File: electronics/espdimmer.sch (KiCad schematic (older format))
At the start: 17 parts, among them J10 Screw_Terminal_01x02, J5 Conn_01x03, J6 Conn_01x02, J7 Screw_Terminal_01x02, J8 Screw_Terminal_01x02, J9 Screw_Terminal_01x02, Q1 IRLB3034, Q2 IRLB3034, SW1 SW_Push, SW2 SW_Push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

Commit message: PCB V1 (narrow)
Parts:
- removed C1: 100n, symbol Device:C_Small
- added C1: CP_Small, Capacitor_Tantalum_SMD:CP_EIA-3216-10_Kemet-I_Pad1.58x1.35mm_HandSolder, symbol Device:CP_Small
- J10: value Screw_Terminal_01x02 -> LED2; footprint (none) -> TerminalBlock:TerminalBlock_bornier-2_P5.08mm
- J5: value Conn_01x03 -> UART; footprint (none) -> Connector_PinHeader_2.54mm:PinHeader_1x03_P2.54mm_Vertical
- J6: value Conn_01x02 -> Motion; footprint (none) -> Connector_PinHeader_2.54mm:PinHeader_1x02_P2.54mm_Vertical
- J7: value Screw_Terminal_01x02 -> PWR1; footprint (none) -> TerminalBlock:TerminalBlock_bornier-2_P5.08mm
- J8: value Screw_Terminal_01x02 -> PWR2; footprint (none) -> TerminalBlock:TerminalBlock_bornier-2_P5.08mm
- J9: value Screw_Terminal_01x02 -> LED1; footprint (none) -> TerminalBlock:TerminalBlock_bornier-2_P5.08mm
- PS1: footprint (none) -> ESPDimmer:XM1584_buck_module
- Q1, Q2: footprint (none) -> Package_TO_SOT_THT:TO-220-3_Vertical
- R1, R2, R3, R4: footprint (none) -> Resistor_SMD:R_0805_2012Metric_Pad1.15x1.40mm_HandSolder
- SW1: value SW_Push -> Reset; footprint (none) -> Button_Switch_THT:SW_PUSH_6mm
- SW2: value SW_Push -> Flash; footprint (none) -> Button_Switch_THT:SW_PUSH_6mm
- U1: footprint (none) -> ESP8266:ESP-01
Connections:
- net labels added: GNDD
- wire segments 64 -> 66
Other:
- moved on the sheet: J10
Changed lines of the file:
@@
 F 0 "U1" H 5600 3850 50  0000 C CNN
 F 1 "ESP-01v090" H 5600 3650 50  0000 C CNN
-F 2 "" H 5600 3700 50  0001 C CNN
+F 2 "ESP8266:ESP-01" H 5600 3700 50  0001 C CNN
 F 3 "http://l0l.org.uk/2014/12/esp8266-modules-hardware-guide-gotta-catch-em-all/" H 5600 3700 50  0001 C CNN
 	1    5600 3700
@@
 F 0 "Q1" H 7504 4096 50  0000 L CNN
 F 1 "IRLB3034" H 7000 4250 50  0000 L CNN
-F 2 "" H 7500 4150 50  0001 C CNN
+F 2 "Package_TO_SOT_THT:TO-220-3_Vertical" H 7500 4150 50  0001 C CNN
 F 3 "~" H 7300 4050 50  0001 C CNN
 	1    7300 4050
@@
 F 0 "Q2" H 7750 3900 50  0000 L CNN
 F 1 "IRLB3034" H 7800 4300 50  0000 L CNN
-F 2 "" H 8100 4150 50  0001 C CNN
+F 2 "Package_TO_SOT_THT:TO-220-3_Vertical" H 8100 4150 50  0001 C CNN
 F 3 "~" H 7900 4050 50  0001 C CNN
 	1    7900 4050
@@
 F 0 "R3" H 7009 3296 50  0000 L CNN
 F 1 "10k" H 7009 3205 50  0000 L CNN
-F 2 "" H 6950 3250 50  0001 C CNN
+F 2 "Resistor_SMD:R_0805_2012Metric_Pad1.15x1.40mm_HandSolder" H 6950 3250 50  0001 C CNN
 F 3 "~" H 6950 3250 50  0001 C CNN
 	1    6950 3250
@@
 F 0 "R4" H 7709 3296 50  0000 L CNN
 F 1 "10k" H 7709 3205 50  0000 L CNN
-F 2 "" H 7650 3250 50  0001 C CNN
+F 2 "Resistor_SMD:R_0805_2012Metric_Pad1.15x1.40mm_HandSolder" H 7650 3250 50  0001 C CNN
 F 3 "~" H 7650 3250 50  0001 C CNN
 	1    7650 3250
@@
 Wire Wire Line
 	6950 2950 6950 3150
-$Comp
-L power:GND #PWR012
-U 1 1 5FDF4073
-P 7400 4550
-F 0 "#PWR012" H 7400 4300 50  0001 C CNN
-F 1 "GND" H 7405 4377 50  0000 C CNN
-F 2 "" H 7400 4550 50  0001 C CNN
-F 3 "" H 7400 4550 50  0001 C CNN
-	1    7400 4550
-	1    0    0    -1
-$EndComp
-$Comp
-L power:GND #PWR014
-U 1 1 5FDF454A
-P 8000 4550
-F 0 "#PWR014" H 8000 4300 50  0001 C CNN
-F 1 "GND" H 8005 4377 50  0000 C CNN
-F 2 "" H 8000 4550 50  0001 C CNN
-F 3 "" H 8000 4550 50  0001 C CNN
-	1    8000 4550
-	1    0    0    -1
-$EndComp
-Wire Wire Line
-	7400 4250 7400 4550
-$Comp
-L power:GND #PWR03
-U 1 1 5FE22A75
-P 3550 4550
-F 0 "#PWR03" H 3550 4300 50  0001 C CNN
-F 1 "GND" H 3555 4377 50  0000 C CNN
-F 2 "" H 3550 4550 50  0001 C CNN
-F 3 "" H 3550 4550 50  0001 C CNN
-	1    3550 4550
-	1    0    0    -1
-$EndComp
+Wire Wire Line
+	7400 4250 7400 4400
 $Comp
 L power:GND #PWR02
 U 1 1 5FE2314A
-P 2650 4550
-F 0 "#PWR02" H 2650 4300 50  0001 C CNN
-F 1 "GND" H 2655 4377 50  0000 C CNN
-F 2 "" H 2650 4550 50  0001 C CNN
-F 3 "" H 2650 4550 50  0001 C CNN
-	1    2650 4550
-	1    0    0    -1
-$EndComp
-Wire Wire Line
-	2650 3850 2650 4550
-Wire Wire Line
-	3550 3850 3550 4550
-$Comp
-L Connector:Screw_Terminal_01x02 J8
-U 1 1 5FE24A4C
-P 8700 3050
-F 0 "J8" H 8850 3000 50  0000 C CNN
-F 1 "Screw_Terminal_01x02" H 8618 3176 50  0001 C CNN
-F 2 "" H 8700 3050 50  0001 C CNN
-F 3 "~" H 8700 3050 50  0001 C CNN
-	1    8700 3050
-	1    0    0    -1
-$EndComp
-$Comp
-L power:GND #PWR015
-U 1 1 5FE25B65
-P 8450 4550
-F 0 "#PWR015" H 8450 4300 50  0001 C CNN
-F 1 "GND" H 8455 4377 50  0000 C CNN
-F 2 "" H 8450 4550 50  0001 C CNN
-F 3 "" H 8450 4550 50  0001 C CNN
-	1    8450 4550
-	1    0    0    -1
-$EndComp
-$Comp
-L Device:C_Small C1
-U 1 1 5FE1F45B
-P 3750 4150
-F 0 "C1" H 3900 4100 50  0000 R CNN
-F 1 "100n" H 3950 4250 50  0000 R CNN
-F 2 "" H 3750 4150 50  0001 C CNN
-F 3 "~" H 3750 4150 50  0001 C CNN
-	1    3750 4150
-	1    0    0    1
-$EndComp
+P 3150 4550
+F 0 "#PWR02" H 3150 4300 50  0001 C CNN
+F 1 "GND" H 3155 4377 50  0000 C CNN
+F 2 "" H 3150 4550 50  0001 C CNN
+F 3 "" H 3150 4550 50  0001 C CNN
+	1    3150 4550
+	1    0    0    -1
+$EndComp
+Wire Wire Line
+	3150 4050 3150 4550
 $Comp
 L power:GND #PWR05
@@
 F 0 "R1" H 4059 3696 50  0000 L CNN
 F 1 "10k" H 4059 3605 50  0000 L CNN
-F 2 "" H 4000 3650 50  0001 C CNN
+F 2 "Resistor_SMD:R_0805_2012Metric_Pad1.15x1.40mm_HandSolder" H 4000 3650 50  0001 C CNN
 F 3 "~" H 4000 3650 50  0001 C CNN
 	1    4000 3650
@@
 F 0 "R2" H 4500 3800 50  0000 L CNN
 F 1 "10k" H 4500 3700 50  0000 L CNN
-F 2 "" H 4350 3750 50  0001 C CNN
+F 2 "Resistor_SMD:R_0805_2012Metric_Pad1.15x1.40mm_HandSolder" H 4350 3750 50  0001 C CNN
 F 3 "~" H 4350 3750 50  0001 C CNN
 	1    4350 3750
@@
 P 4550 4300
 F 0 "SW1" V 4504 4252 50  0000 R CNN
-F 1 "SW_Push" V 4595 4252 50  0001 R CNN
-F 2 "" H 4550 4500 50  0001 C CNN
+F 1 "Reset" V 4595 4252 50  0000 R CNN
+F 2 "Button_Switch_THT:SW_PUSH_6mm" H 4550 4500 50  0001 C CNN
 F 3 "~" H 4550 4500 50  0001 C CNN
 	1    4550 4300
@@
 L Connector:Screw_Terminal_01x02 J9
 U 1 1 5FE61684
-P 8700 3350
-F 0 "J9" H 8850 3300 50  0000 C CNN
-F 1 "Screw_Terminal_01x02" H 8618 3476 50  0001 C CNN
-F 2 "" H 8700 3350 50  0001 C CNN
-F 3 "~" H 8700 3350 50  0001 C CNN
-	1    8700 3350
-	1    0    0    -1
+P 8700 3450
+F 0 "J9" H 8850 3350 50  0000 C CNN
+F 1 "LED1" H 8900 3450 50  0000 C CNN
+F 2 "TerminalBlock:TerminalBlock_bornier-2_P5.08mm" H 8700 3450 50  0001 C CNN
+F 3 "~" H 8700 3450 50  0001 C CNN
+	1    8700 3450
+	1    0    0    1
 $EndComp
 $Comp
@@
 U 1 1 5FE62049
 P 8700 3750
-F 0 "J10" H 8850 3700 50  0000 C CNN
-F 1 "Screw_Terminal_01x02" H 8618 3876 50  0001 C CNN
-F 2 "" H 8700 3750 50  0001 C CNN
+F 0 "J10" H 8900 3650 50  0000 C CNN
+F 1 "LED2" H 8900 3750 50  0000 C CNN
+F 2 "TerminalBlock:TerminalBlock_bornier-2_P5.08mm" H 8700 3750 50  0001 C CNN
 F 3 "~" H 8700 3750 50  0001 C CNN
 	1    8700 3750
-	1    0    0    -1
+	1    0    0    1
 $EndComp
 $Comp
@@
 P 6950 4300
 F 0 "SW2" V 6904 4252 50  0000 R CNN
-F 1 "SW_Push" V 6995 4252 50  0001 R CNN
-F 2 "" H 6950 4500 50  0001 C CNN
+F 1 "Flash" V 6995 4252 50  0000 R CNN
+F 2 "Button_Switch_THT:SW_PUSH_6mm" H 6950 4500 50  0001 C CNN
 F 3 "~" H 6950 4500 50  0001 C CNN
 	1    6950 4300
@@
 	6950 4100 6950 4050
 Connection ~ 6950 4050
-Wire Wire Line
-	8500 3850 8000 3850
 Wire Wire Line
 	8500 3450 7400 3450
@@
 P 6150 2700
 F 0 "J6" V 6250 2650 50  0000 C CNN
-F 1 "Conn_01x02" H 6300 2850 50  0001 C CNN
-F 2 "" H 6150 2700 50  0001 C CNN
+F 1 "Motion" V 6150 2900 50  0000 C CNN
+F 2 "Connector_PinHeader_2.54mm:PinHeader_1x02_P2.54mm_Vertical" H 6150 2700 50  0001 C CNN
 F 3 "~" H 6150 2700 50  0001 C CNN
 	1    6150 2700
@@
 Connection ~ 8450 3150
 Wire Wire Line
-	8500 3750 8350 3750
-Wire Wire Line
-	8350 3750 8350 3050
+	8500 3650 8350 3650
+Wire Wire Line
+	8350 3650 8350 3050
 Wire Wire Line
 	8350 3050 8500 3050
@@
 P 5650 2700
 F 0 "J5" V 5750 2750 50  0000 R CNN
-F 1 "Conn_01x03" V 5523 2512 50  0001 R CNN
-F 2 "" H 5650 2700 50  0001 C CNN
+F 1 "UART" V 5650 3100 50  0000 R CNN
+F 2 "Connector_PinHeader_2.54mm:PinHeader_1x03_P2.54mm_Vertical" H 5650 2700 50  0001 C CNN
 F 3 "~" H 5650 2700 50  0001 C CNN
 	1    5650 2700
@@
 L Connector:Screw_Terminal_01x02 J7
 U 1 1 5FF5CAAF
-P 8700 2750
-F 0 "J7" H 8850 2700 50  0000 C CNN
-F 1 "Screw_Terminal_01x02" H 8618 2876 50  0001 C CNN
-F 2 "" H 8700 2750 50  0001 C CNN
-F 3 "~" H 8700 2750 50  0001 C CNN
-	1    8700 2750
-	1    0    0    -1
+P 8700 2850
+F 0 "J7" H 8850 2750 50  0000 C CNN
+F 1 "PWR1" H 8900 2850 50  0000 C CNN
+F 2 "TerminalBlock:TerminalBlock_bornier-2_P5.08mm" H 8700 2850 50  0001 C CNN
+F 3 "~" H 8700 2850 50  0001 C CNN
+	1    8700 2850
+	1    0    0    1
 $EndComp
 Wire Wire Line
@@
 F 0 "PS1" H 3150 4117 50  0000 C CNN
 F 1 "BUCK" H 3150 4026 50  0000 C CNN
-F 2 "" H 2100 3500 50  0001 L CNN
+F 2 "ESPDimmer:XM1584_buck_module" H 2100 3500 50  0001 L CNN
 F 3 "" H 4200 3450 50  0001 L CNN
 	1    3150 3750
@@
 $EndComp
 Wire Wire Line
-	2650 3850 2750 3850
-Wire Wire Line
 	2650 3050 8250 3050
 Wire Wire Line
@@
 Wire Wire Line
 	8250 3050 8250 2750
+$Comp
+L Device:CP_Small C1
+U 1 1 5FFA4758
+P 3750 4150
+F 0 "C1" H 3838 4196 50  0000 L CNN
+F 1 "CP_Small" H 3838 4105 50  0000 L CNN
+F 2 "Capacitor_Tantalum_SMD:CP_EIA-3216-10_Kemet-I_Pad1.58x1.35mm_HandSolder" H 3750 4150 50  0001 C CNN
+F 3 "~" H 3750 4150 50  0001 C CNN
+	1    3750 4150
+	1    0    0    -1
+$EndComp
+Wire Wire Line
+	8500 3750 8000 3750
+Wire Wire Line
+	8000 3750 8000 3850
+$Comp
+L Connector:Screw_Terminal_01x02 J8
+U 1 1 5FE24A4C
+P 8700 3150
+F 0 "J8" H 8850 3050 50  0000 C CNN
+F 1 "PWR2" H 8900 3150 50  0000 C CNN
+F 2 "TerminalBlock:TerminalBlock_bornier-2_P5.08mm" H 8700 3150 50  0001 C CNN
+F 3 "~" H 8700 3150 50  0001 C CNN
+	1    8700 3150
+	1    0    0    1
+$EndComp
+$Comp
+L power:GNDD #PWR0101
+U 1 1 5FFD72B4
+P 7400 4550
+F 0 "#PWR0101" H 7400 4300 50  0001 C CNN
+F 1 "GNDD" H 7404 4395 50  0000 C CNN
+F 2 "" H 7400 4550 50  0001 C CNN
+F 3 "" H 7400 4550 50  0001 C CNN
+	1    7400 4550
+	1    0    0    -1
+$EndComp
+$Comp
+L power:GNDD #PWR0102
+U 1 1 5FFD779F
+P 8000 4550
+F 0 "#PWR0102" H 8000 4300 50  0001 C CNN
+F 1 "GNDD" H 8004 4395 50  0000 C CNN
+F 2 "" H 8000 4550 50  0001 C CNN
+F 3 "" H 8000 4550 50  0001 C CNN
+	1    8000 4550
+	1    0    0    -1
+$EndComp
+$Comp
+L power:GNDD #PWR0103
+U 1 1 5FFD7CBE
+P 8450 4550
+F 0 "#PWR0103" H 8450 4300 50  0001 C CNN
+F 1 "GNDD" H 8454 4395 50  0000 C CNN
+F 2 "" H 8450 4550 50  0001 C CNN
+F 3 "" H 8450 4550 50  0001 C CNN
+	1    8450 4550
+	1    0    0    -1
+$EndComp
+$Comp
+L power:GND #PWR0104
+U 1 1 5FFD8056
+P 7200 4550
+F 0 "#PWR0104" H 7200 4300 50  0001 C CNN
+F 1 "GND" H 7205 4377 50  0000 C CNN
+F 2 "" H 7200 4550 50  0001 C CNN
+F 3 "" H 7200 4550 50  0001 C CNN
+	1    7200 4550
+	1    0    0    -1
+$EndComp
+Wire Wire Line
+	7200 4550 7200 4400
+Wire Wire Line
+	7200 4400 7400 4400
+Connection ~ 7400 4400
+Wire Wire Line
+	7400 4400 7400 4550
 $EndSCHEMATC

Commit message: Schematics and PCB design updated
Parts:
- removed PS1: BUCK, ESPDimmer:XM1584_buck_module, symbol buck:BUCK
- added PS1: BUCK_4P, Buck:XM1584_buck_mod_4p, symbol Buck:BUCK_4P
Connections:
- net labels added: PWR1, PWR2
- wire segments 66 -> 64
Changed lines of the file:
@@
 Wire Wire Line
 	6950 2950 6950 3150
-Wire Wire Line
-	7400 4250 7400 4400
 $Comp
 L power:GND #PWR02
 U 1 1 5FE2314A
-P 3150 4550
-F 0 "#PWR02" H 3150 4300 50  0001 C CNN
-F 1 "GND" H 3155 4377 50  0000 C CNN
-F 2 "" H 3150 4550 50  0001 C CNN
-F 3 "" H 3150 4550 50  0001 C CNN
-	1    3150 4550
-	1    0    0    -1
-$EndComp
-Wire Wire Line
-	3150 4050 3150 4550
+P 3550 4550
+F 0 "#PWR02" H 3550 4300 50  0001 C CNN
+F 1 "GND" H 3555 4377 50  0000 C CNN
+F 2 "" H 3550 4550 50  0001 C CNN
+F 3 "" H 3550 4550 50  0001 C CNN
+	1    3550 4550
+	1    0    0    -1
+$EndComp
+Wire Wire Line
+	3550 3850 3550 4550
 $Comp
 L power:GND #PWR05
@@
 Wire Wire Line
 	2650 3050 2650 3650
-$Comp
-L buck:BUCK PS1
-U 1 1 5FF86192
-P 3150 3750
-F 0 "PS1" H 3150 4117 50  0000 C CNN
-F 1 "BUCK" H 3150 4026 50  0000 C CNN
-F 2 "ESPDimmer:XM1584_buck_module" H 2100 3500 50  0001 L CNN
-F 3 "" H 4200 3450 50  0001 L CNN
-	1    3150 3750
-	1    0    0    -1
-$EndComp
 Wire Wire Line
 	2650 3050 8250 3050
@@
 $EndComp
 $Comp
-L power:GND #PWR0104
-U 1 1 5FFD8056
-P 7200 4550
-F 0 "#PWR0104" H 7200 4300 50  0001 C CNN
-F 1 "GND" H 7205 4377 50  0000 C CNN
-F 2 "" H 7200 4550 50  0001 C CNN
-F 3 "" H 7200 4550 50  0001 C CNN
-	1    7200 4550
-	1    0    0    -1
-$EndComp
-Wire Wire Line
-	7200 4550 7200 4400
-Wire Wire Line
-	7200 4400 7400 4400
-Connection ~ 7400 4400
-Wire Wire Line
-	7400 4400 7400 4550
+L Buck:BUCK_4P PS1
+U 1 1 6006370D
+P 3150 3750
+F 0 "PS1" H 3150 4117 50  0000 C CNN
+F 1 "BUCK_4P" H 3150 4026 50  0000 C CNN
+F 2 "Buck:XM1584_buck_mod_4p" H 2100 3500 50  0001 L CNN
+F 3 "" H 4200 3450 50  0001 L CNN
+	1    3150 3750
+	1    0    0    -1
+$EndComp
+$Comp
+L power:GNDD #PWR0105
+U 1 1 60068775
+P 2750 4550
+F 0 "#PWR0105" H 2750 4300 50  0001 C CNN
+F 1 "GNDD" H 2754 4395 50  0000 C CNN
+F 2 "" H 2750 4550 50  0001 C CNN
+F 3 "" H 2750 4550 50  0001 C CNN
+	1    2750 4550
+	1    0    0    -1
+$EndComp
+Wire Wire Line
+	2750 3850 2750 4550
+Wire Wire Line
+	7400 4250 7400 4550
+Text Label 8250 2750 0    50   ~ 0
+PWR1
+Text Label 8350 3050 3    50   ~ 0
+PWR2
 $EndSCHEMATC

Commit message: Schematics/PCB updated
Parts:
- added R5: 4.7k, Resistor_SMD:R_0805_2012Metric_Pad1.15x1.40mm_HandSolder, symbol Device:R_Small
- R3, R4: value 10k -> 4.7k
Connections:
- wire segments 64 -> 66
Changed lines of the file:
@@
 P 6950 3250
 F 0 "R3" H 7009 3296 50  0000 L CNN
-F 1 "10k" H 7009 3205 50  0000 L CNN
+F 1 "4.7k" H 7009 3205 50  0000 L CNN
 F 2 "Resistor_SMD:R_0805_2012Metric_Pad1.15x1.40mm_HandSolder" H 6950 3250 50  0001 C CNN
 F 3 "~" H 6950 3250 50  0001 C CNN
@@
 P 7650 3250
 F 0 "R4" H 7709 3296 50  0000 L CNN
-F 1 "10k" H 7709 3205 50  0000 L CNN
+F 1 "4.7k" H 7709 3205 50  0000 L CNN
 F 2 "Resistor_SMD:R_0805_2012Metric_Pad1.15x1.40mm_HandSolder" H 7650 3250 50  0001 C CNN
 F 3 "~" H 7650 3250 50  0001 C CNN
@@
 Text Label 8350 3050 3    50   ~ 0
 PWR2
+$Comp
+L Device:R_Small R5
+U 1 1 600883F6
+P 6800 2950
+F 0 "R5" H 6859 2996 50  0000 L CNN
+F 1 "4.7k" H 6859 2905 50  0000 L CNN
+F 2 "Resistor_SMD:R_0805_2012Metric_Pad1.15x1.40mm_HandSolder" H 6800 2950 50  0001 C CNN
+F 3 "~" H 6800 2950 50  0001 C CNN
+	1    6800 2950
+	0    1    -1   0
+$EndComp
+Wire Wire Line
+	6650 2950 6700 2950
+Connection ~ 6650 2950
+Wire Wire Line
+	6900 2950 6950 2950
 $EndSCHEMATC

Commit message: esphome config added
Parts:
- added C2: 100nF 50V, Capacitor_SMD:C_0805_2012Metric_Pad1.15x1.40mm_HandSolder, symbol Device:C_Small
- added D1: SS14, Diode_SMD:D_SMA_Handsoldering, symbol Device:D_Small
- C1: value CP_Small -> 10uF 10V
- U1: symbol ESP-8266:ESP-01v090 -> espdimmer-rescue:ESP-01v090-ESP-8266
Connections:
- net labels removed: GNDD
- wire segments 66 -> 69
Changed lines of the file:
@@
 $EndDescr
 $Comp
-L ESP-8266:ESP-01v090 U1
+L espdimmer-rescue:ESP-01v090-ESP-8266 U1
 U 1 1 5FDE3173
 P 5600 3700
@@
 	1    0    0    -1
 $EndComp
-Wire Wire Line
-	3550 3850 3550 4550
 $Comp
 L power:GND #PWR05
@@
 	4100 3650 4650 3650
 Wire Wire Line
-	2650 3650 2750 3650
+	2500 3650 2750 3650
 Wire Wire Line
 	6950 3750 6950 4050
@@
 $EndComp
 Wire Wire Line
-	2650 3050 2650 3650
-Wire Wire Line
-	2650 3050 8250 3050
+	2500 3050 2500 3650
+Wire Wire Line
+	2500 3050 7900 3050
 Wire Wire Line
 	8250 3350 8250 3050
@@
 P 3750 4150
 F 0 "C1" H 3838 4196 50  0000 L CNN
-F 1 "CP_Small" H 3838 4105 50  0000 L CNN
+F 1 "10uF 10V" H 3838 4105 50  0000 L CNN
 F 2 "Capacitor_Tantalum_SMD:CP_EIA-3216-10_Kemet-I_Pad1.58x1.35mm_HandSolder" H 3750 4150 50  0001 C CNN
 F 3 "~" H 3750 4150 50  0001 C CNN
@@
 $EndComp
 $Comp
-L power:GNDD #PWR0101
-U 1 1 5FFD72B4
-P 7400 4550
-F 0 "#PWR0101" H 7400 4300 50  0001 C CNN
-F 1 "GNDD" H 7404 4395 50  0000 C CNN
-F 2 "" H 7400 4550 50  0001 C CNN
-F 3 "" H 7400 4550 50  0001 C CNN
-	1    7400 4550
-	1    0    0    -1
-$EndComp
-$Comp
-L power:GNDD #PWR0102
-U 1 1 5FFD779F
-P 8000 4550
-F 0 "#PWR0102" H 8000 4300 50  0001 C CNN
-F 1 "GNDD" H 8004 4395 50  0000 C CNN
-F 2 "" H 8000 4550 50  0001 C CNN
-F 3 "" H 8000 4550 50  0001 C CNN
-	1    8000 4550
-	1    0    0    -1
-$EndComp
-$Comp
-L power:GNDD #PWR0103
-U 1 1 5FFD7CBE
-P 8450 4550
-F 0 "#PWR0103" H 8450 4300 50  0001 C CNN
-F 1 "GNDD" H 8454 4395 50  0000 C CNN
-F 2 "" H 8450 4550 50  0001 C CNN
-F 3 "" H 8450 4550 50  0001 C CNN
-	1    8450 4550
-	1    0    0    -1
-$EndComp
-$Comp
 L Buck:BUCK_4P PS1
 U 1 1 6006370D
@@
 	1    0    0    -1
 $EndComp
-$Comp
-L power:GNDD #PWR0105
-U 1 1 60068775
-P 2750 4550
-F 0 "#PWR0105" H 2750 4300 50  0001 C CNN
-F 1 "GNDD" H 2754 4395 50  0000 C CNN
-F 2 "" H 2750 4550 50  0001 C CNN
-F 3 "" H 2750 4550 50  0001 C CNN
-	1    2750 4550
-	1    0    0    -1
-$EndComp
-Wire Wire Line
-	2750 3850 2750 4550
 Wire Wire Line
 	7400 4250 7400 4550
@@
 Wire Wire Line
 	6900 2950 6950 2950
+$Comp
+L Device:D_Small D1
+U 1 1 600C3ECC
+P 8000 3050
+F 0 "D1" H 8000 3255 50  0000 C CNN
+F 1 "SS14" H 8000 3164 50  0000 C CNN
+F 2 "Diode_SMD:D_SMA_Handsoldering" V 8000 3050 50  0001 C CNN
+F 3 "~" V 8000 3050 50  0001 C CNN
+	1    8000 3050
+	1    0    0    -1
+$EndComp
+Wire Wire Line
+	8100 3050 8250 3050
+Wire Wire Line
+	2500 4050 2500 3650
+Connection ~ 2500 3650
+Wire Wire Line
+	2500 4550 2500 4250
+$Comp
+L Device:C_Small C2
+U 1 1 600E829E
+P 2500 4150
+F 0 "C2" H 2592 4196 50  0000 L CNN
+F 1 "100nF 50V" H 2250 4050 50  0000 L CNN
+F 2 "Capacitor_SMD:C_0805_2012Metric_Pad1.15x1.40mm_HandSolder" H 2500 4150 50  0001 C CNN
+F 3 "~" H 2500 4150 50  0001 C CNN
+	1    2500 4150
+	1    0    0    -1
+$EndComp
+$Comp
+L power:GND #PWR0101
+U 1 1 600F7AD4
+P 2750 4550
+F 0 "#PWR0101" H 2750 4300 50  0001 C CNN
+F 1 "GND" H 2755 4377 50  0000 C CNN
+F 2 "" H 2750 4550 50  0001 C CNN
+F 3 "" H 2750 4550 50  0001 C CNN
+	1    2750 4550
+	1    0    0    -1
+$EndComp
+$Comp
+L power:GND #PWR0102
+U 1 1 600F7DB2
+P 2500 4550
+F 0 "#PWR0102" H 2500 4300 50  0001 C CNN
+F 1 "GND" H 2505 4377 50  0000 C CNN
+F 2 "" H 2500 4550 50  0001 C CNN
+F 3 "" H 2500 4550 50  0001 C CNN
+	1    2500 4550
+	1    0    0    -1
+$EndComp
+Wire Wire Line
+	2750 3850 2750 4550
+Wire Wire Line
+	3550 3850 3550 4550
+$Comp
+L power:GND #PWR0103
+U 1 1 600FCBBD
+P 7400 4550
+F 0 "#PWR0103" H 7400 4300 50  0001 C CNN
+F 1 "GND" H 7405 4377 50  0000 C CNN
+F 2 "" H 7400 4550 50  0001 C CNN
+F 3 "" H 7400 4550 50  0001 C CNN
+	1    7400 4550
+	1    0    0    -1
+$EndComp
+$Comp
+L power:GND #PWR0104
+U 1 1 600FCEBE
+P 8000 4550
+F 0 "#PWR0104" H 8000 4300 50  0001 C CNN
+F 1 "GND" H 8005 4377 50  0000 C CNN
+F 2 "" H 8000 4550 50  0001 C CNN
+F 3 "" H 8000 4550 50  0001 C CNN
+	1    8000 4550
+	1    0    0    -1
+$EndComp
+$Comp
+L power:GND #PWR0105
+U 1 1 600FD215
+P 8450 4550
+F 0 "#PWR0105" H 8450 4300 50  0001 C CNN
+F 1 "GND" H 8455 4377 50  0000 C CNN
+F 2 "" H 8450 4550 50  0001 C CNN
+F 3 "" H 8450 4550 50  0001 C CNN
+	1    8450 4550
+	1    0    0    -1
+$EndComp
 $EndSCHEMATC

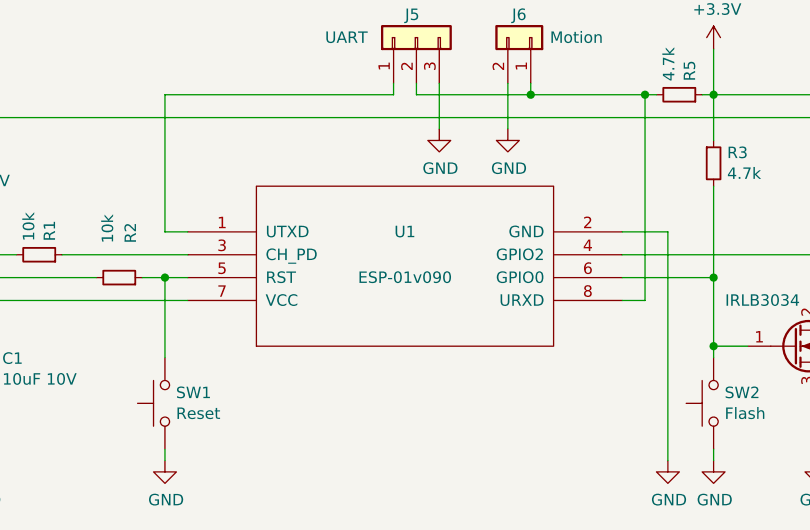
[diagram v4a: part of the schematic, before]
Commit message: switched to internal esp8266 libs
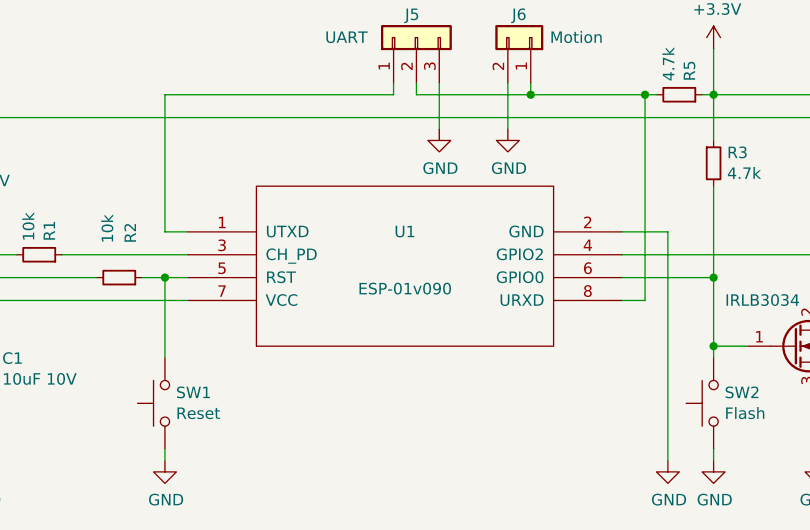
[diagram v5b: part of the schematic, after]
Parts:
- removed U1: ESP-01v090, ESP8266:ESP-01, symbol espdimmer-rescue:ESP-01v090-ESP-8266
- added U1: ESP-01v090, ESP8266:ESP-01, symbol esp8266:ESP-01v090
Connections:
- net +3V3: now also U1.7 (VCC)
- net GND: now also U1.2 (GND)
- net at J5.1 (Pin_1): now also U1.1 (UTXD)
- net at R1.1: now also U1.3 (CH_PD)
- net at Q2.1 (G), R4.2: now also U1.4 (GPIO2)
- net at R2.1, SW1.1: now also U1.5 (RST)
- net at Q1.1 (G), R3.2, SW2.1: now also U1.6 (GPIO0)
- net at J5.2 (Pin_2), J6.1 (Pin_1), R5.2: now also U1.8 (URXD)
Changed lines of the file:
@@
 $EndDescr
-$Comp
-L espdimmer-rescue:ESP-01v090-ESP-8266 U1
-U 1 1 5FDE3173
-P 5600 3700
-F 0 "U1" H 5600 3850 50  0000 C CNN
-F 1 "ESP-01v090" H 5600 3650 50  0000 C CNN
-F 2 "ESP8266:ESP-01" H 5600 3700 50  0001 C CNN
-F 3 "http://l0l.org.uk/2014/12/esp8266-modules-hardware-guide-gotta-catch-em-all/" H 5600 3700 50  0001 C CNN
-	1    5600 3700
-	1    0    0    -1
-$EndComp
 $Comp
 L Device:Q_NMOS_GDS Q1
@@
 	1    0    0    -1
 $EndComp
+$Comp
+L esp8266:ESP-01v090 U1
+U 1 1 609D5C23
+P 5600 3700
+F 0 "U1" H 5600 3850 50  0000 C CNN
+F 1 "ESP-01v090" H 5600 3600 50  0000 C CNN
+F 2 "ESP8266:ESP-01" H 5600 3700 50  0001 C CNN
+F 3 "http://l0l.org.uk/2014/12/esp8266-modules-hardware-guide-gotta-catch-em-all/" H 5600 3700 50  0001 C CNN
+	1    5600 3700
+	1    0    0    -1
+$EndComp
